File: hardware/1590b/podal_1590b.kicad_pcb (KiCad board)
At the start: 2 copper layers, 55 x 84 mm, 56 parts, among them J1 Guitar in, J2 fsw pin 1, J3 fsw pin 2, J4 fsw pin 4, J5 fsw pin 5, J6 fsw pin 6, J7 Left out, J8 Right out, J9 fsw pin 3, SW1 Switch 1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

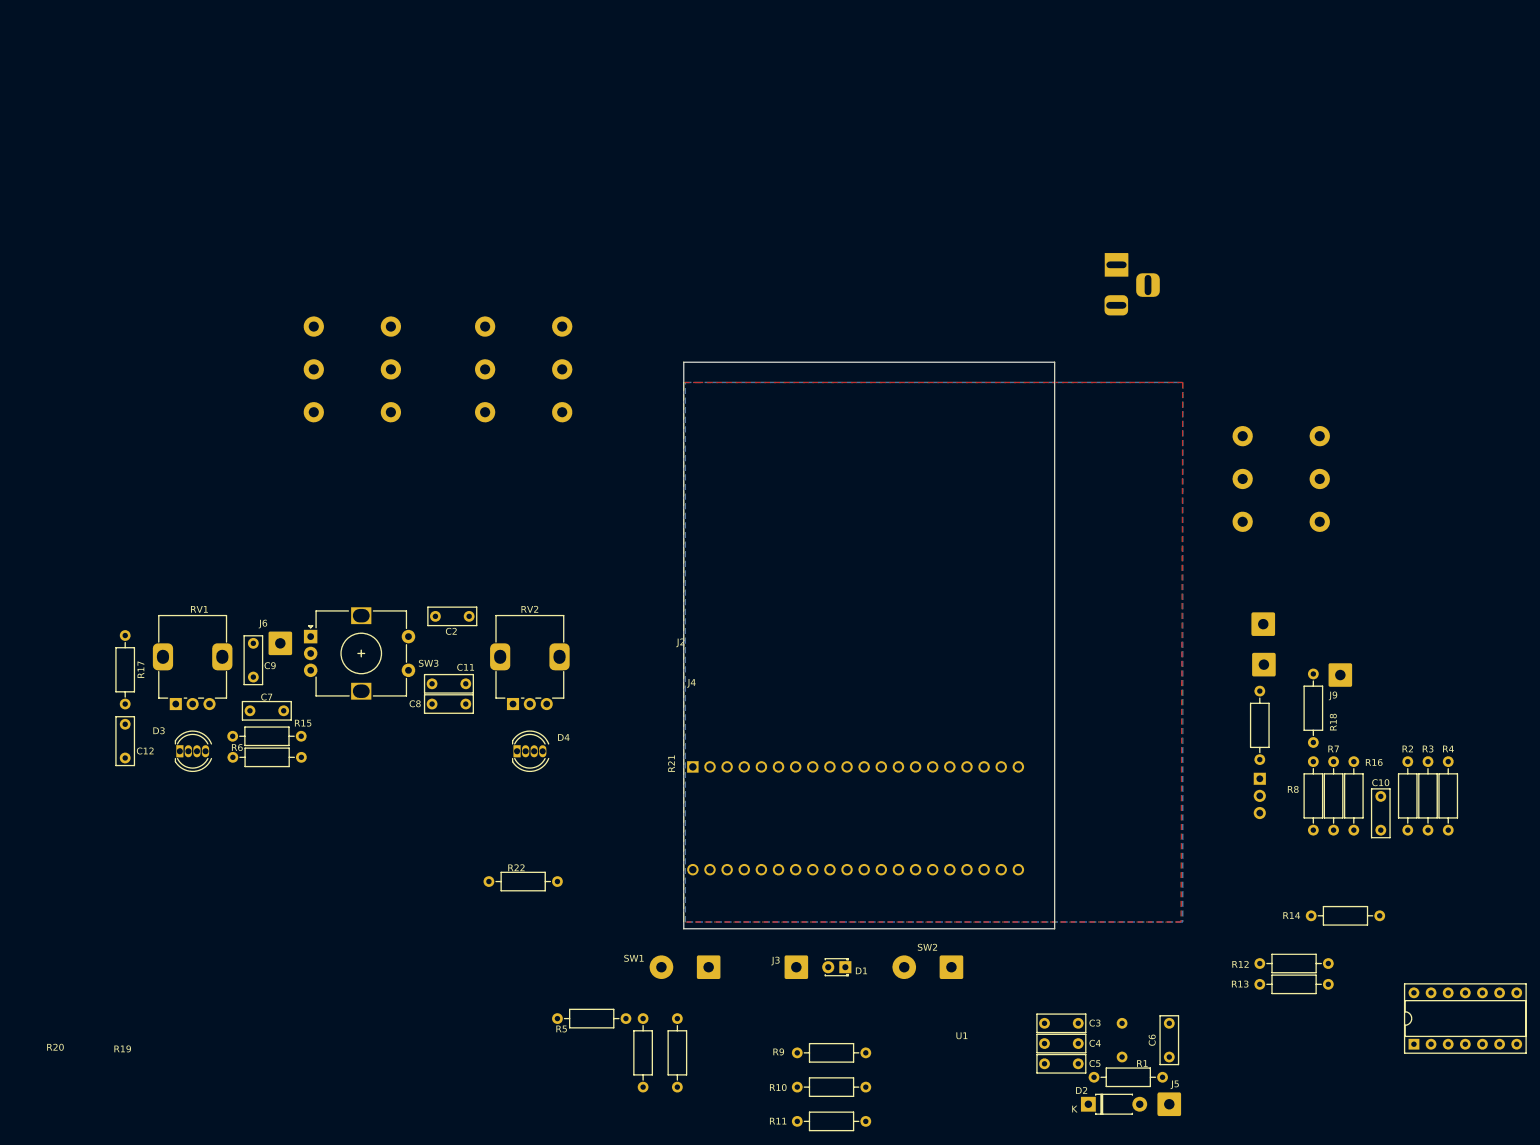
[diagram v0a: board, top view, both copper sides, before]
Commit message: Compressor working with sensible led output
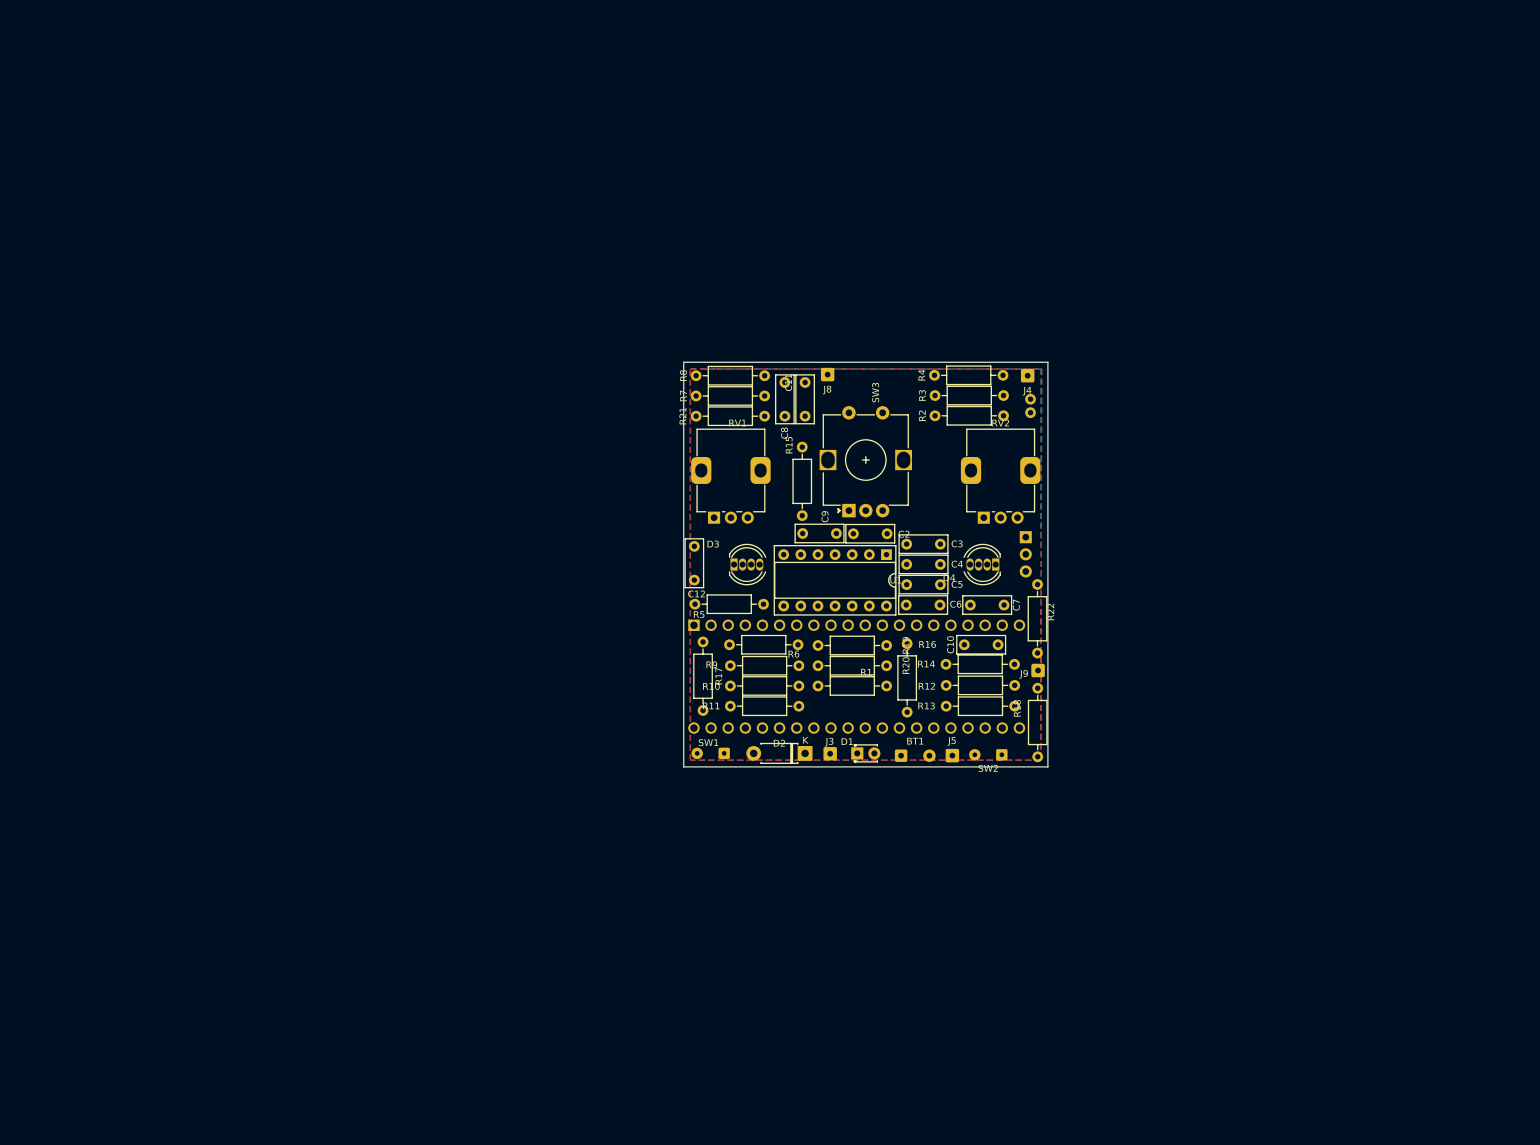
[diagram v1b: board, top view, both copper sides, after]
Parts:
- removed J1: Guitar in, Connector_Audio:Jack_6.35mm_Neutrik_NRJ6HM-1_Horizontal
- removed J2: fsw pin 1, Connector_Wire:SolderWire-0.75sqmm_1x01_D1.25mm_OD3.5mm
- removed J6: fsw pin 6, Connector_Wire:SolderWire-0.75sqmm_1x01_D1.25mm_OD3.5mm
- removed J7: Left out, Connector_Audio:Jack_6.35mm_Neutrik_NRJ6HM-1_Horizontal
- BT1: footprint Connector_BarrelJack:BarrelJack_Horizontal_centre_negative -> Connector_Wire:SolderWire-0.25sqmm_1x02_P4.2mm_D0.65mm_OD1.7mm; moved to F.Cu
- C1: footprint Capacitor_THT:C_Radial_D10.0mm_H16.0mm_P5.00mm -> Capacitor_THT:C_Radial_D5.0mm_H11.0mm_P2.00mm
- J3, J4, J5, J9: footprint Connector_Wire:SolderWire-0.75sqmm_1x01_D1.25mm_OD3.5mm -> Connector_Wire:SolderWire-0.25sqmm_1x01_D0.65mm_OD2mm
- J8: footprint Connector_Audio:Jack_6.35mm_Neutrik_NRJ6HM-1_Horizontal -> Connector_Wire:SolderWire-0.25sqmm_1x01_D0.65mm_OD2mm; moved to F.Cu
- SW1, SW2: footprint Connector_Wire:SolderWire-0.75sqmm_1x02_P7mm_D1.25mm_OD3.5mm -> Connector_Wire:SolderWire-0.15sqmm_1x02_P4mm_D0.5mm_OD1.5mm
- moved R7 109.0 mm to (101.8, 55.0), turned to 0 degrees
- moved C7 108.0 mm to (147.5, 86.0)
- moved U1 106.7 mm to (130.1, 78.5), turned to -90 degrees
- moved R8 105.6 mm to (112.0, 52.0), turned to 180 degrees
- moved R21 97.9 mm to (101.8, 58.0), turned to 0 degrees
- moved R4 95.3 mm to (137.2, 51.9), turned to 0 degrees
- moved C1 93.5 mm to (151.4, 55.5)
- moved R3 91.0 mm to (137.3, 54.9), turned to 0 degrees
- moved R15 90.6 mm to (117.6, 72.7), turned to 90 degrees
- moved C9 89.0 mm to (122.6, 75.4), turned to 180 degrees
- moved C12 88.4 mm to (101.6, 82.3)
- moved D3 86.7 mm to (107.5, 80.0)
- moved R2 85.8 mm to (147.4, 57.9), turned to 180 degrees
- moved R17 85.7 mm to (102.9, 91.5)
- moved RV1 84.5 mm to (104.5, 73.0)
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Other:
- board size 55 x 84 mm -> 54 x 60 mm
- board text added: "Podal v0.3 Denis Crowdy"
- board text removed: "Podal v0.2 Denis Crowdy"

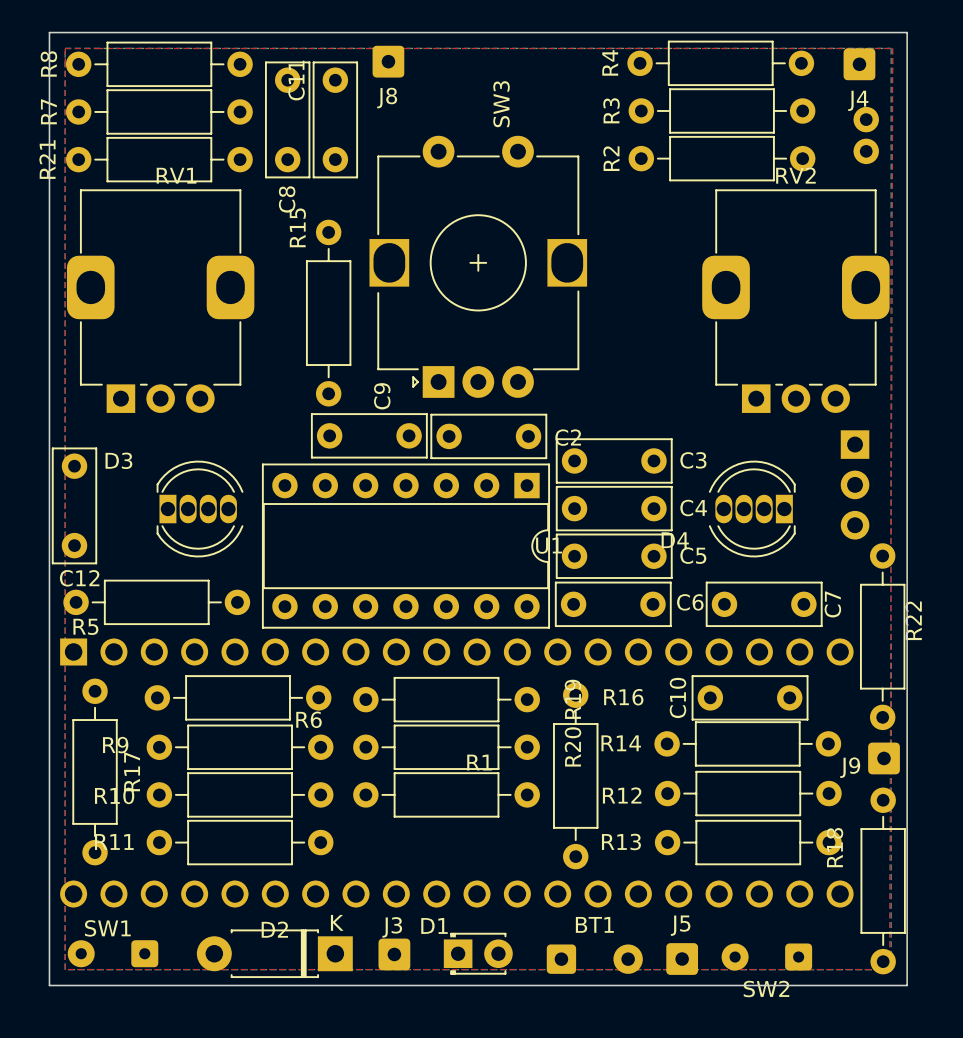
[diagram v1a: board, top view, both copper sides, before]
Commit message: Start work on connecting traces
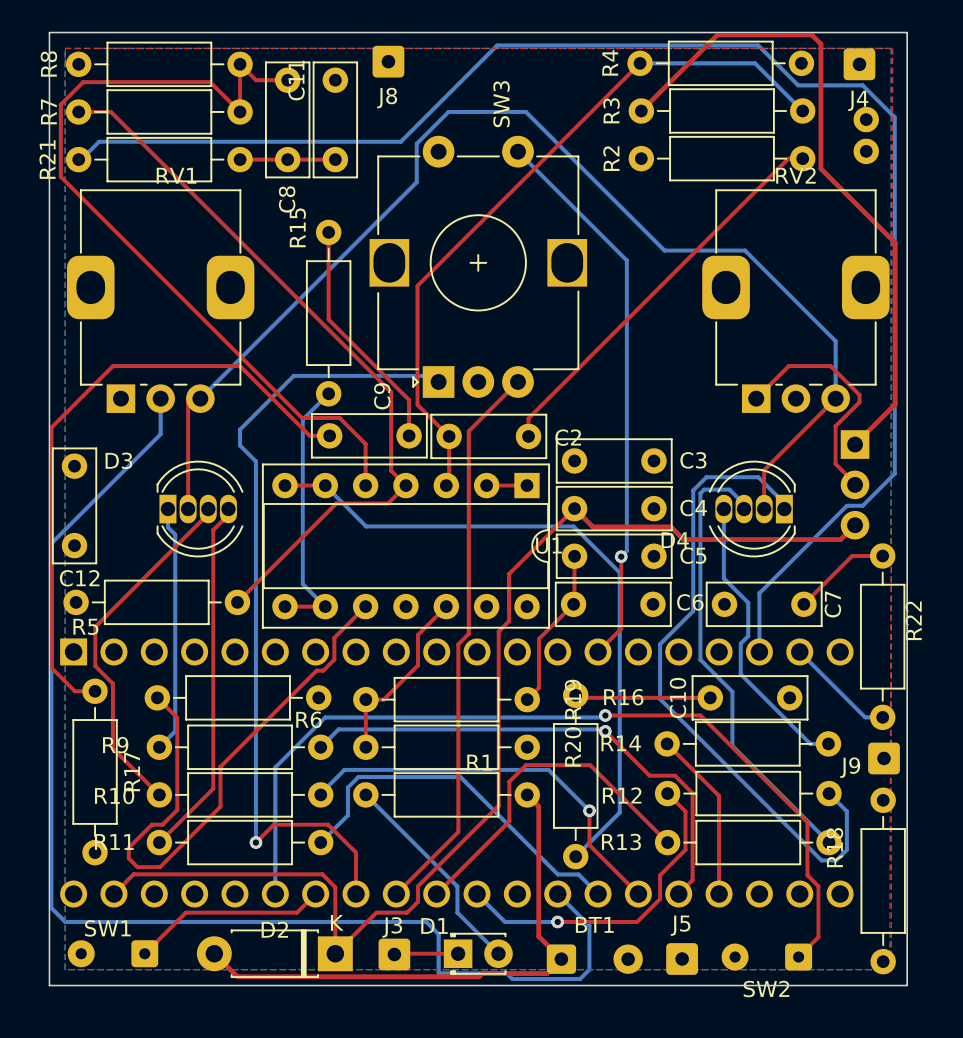
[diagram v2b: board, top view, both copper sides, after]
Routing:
- net +5V: track 0.00 -> 98.9 mm
- net /Left out: track 0.00 -> 94.0 mm
- net Net-(A1-ADC_6): track 0.00 -> 77.9 mm
- net /VCC: track 0.00 -> 75.4 mm
- net /3v3: track 0.00 -> 74.9 mm
- net Net-(A1-SAI2_SCK): track 0.00 -> 54.9 mm, vias 0 -> 1
- net Net-(U1B-+): track 0.00 -> 52.4 mm
- net Net-(A1-SAI2_SD_A): track 0.00 -> 51.5 mm, vias 0 -> 1
- net Net-(U1A-+): track 0.00 -> 44.8 mm
- net Net-(U1B--): track 0.00 -> 42.4 mm
- net Net-(D4-RK): track 0.00 -> 41.4 mm
- net Net-(C9-Pad2): track 0.00 -> 39.4 mm
- net Net-(U1C-+): track 0.00 -> 37.0 mm
- net Net-(A1-SAI2_SD_B): track 0.00 -> 35.4 mm
- net /ENC_CLICK: track 0.00 -> 35.1 mm, vias 0 -> 1
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
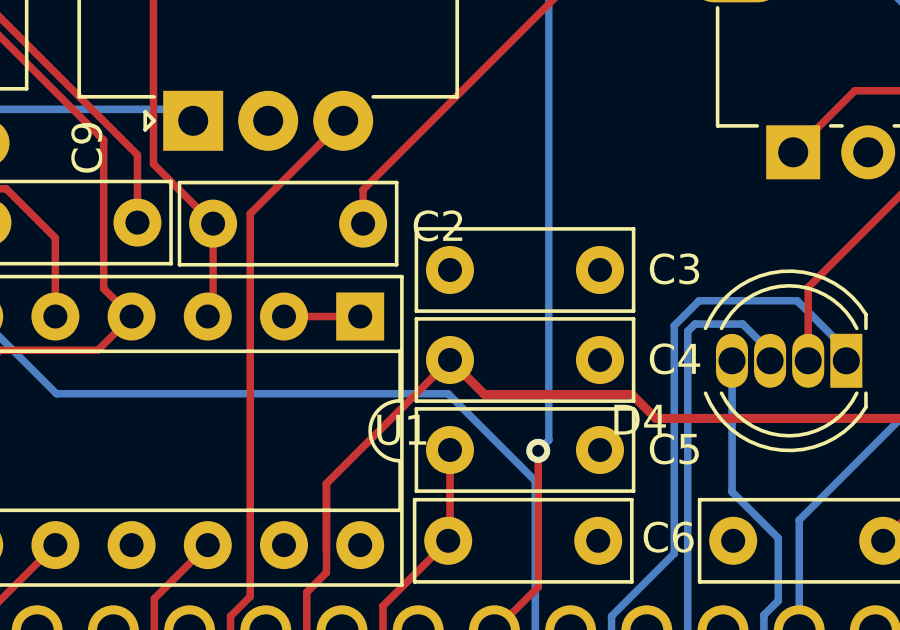
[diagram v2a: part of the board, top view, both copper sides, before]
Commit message: See if we can get some icad compatibility between mac and linux
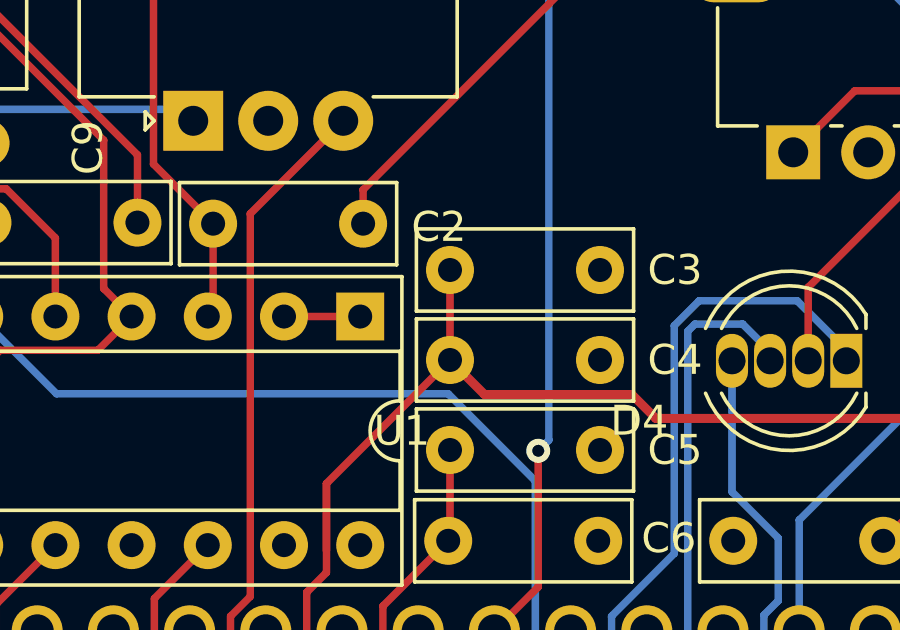
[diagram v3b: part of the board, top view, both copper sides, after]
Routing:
- net /VCC: track 75.4 -> 78.4 mm

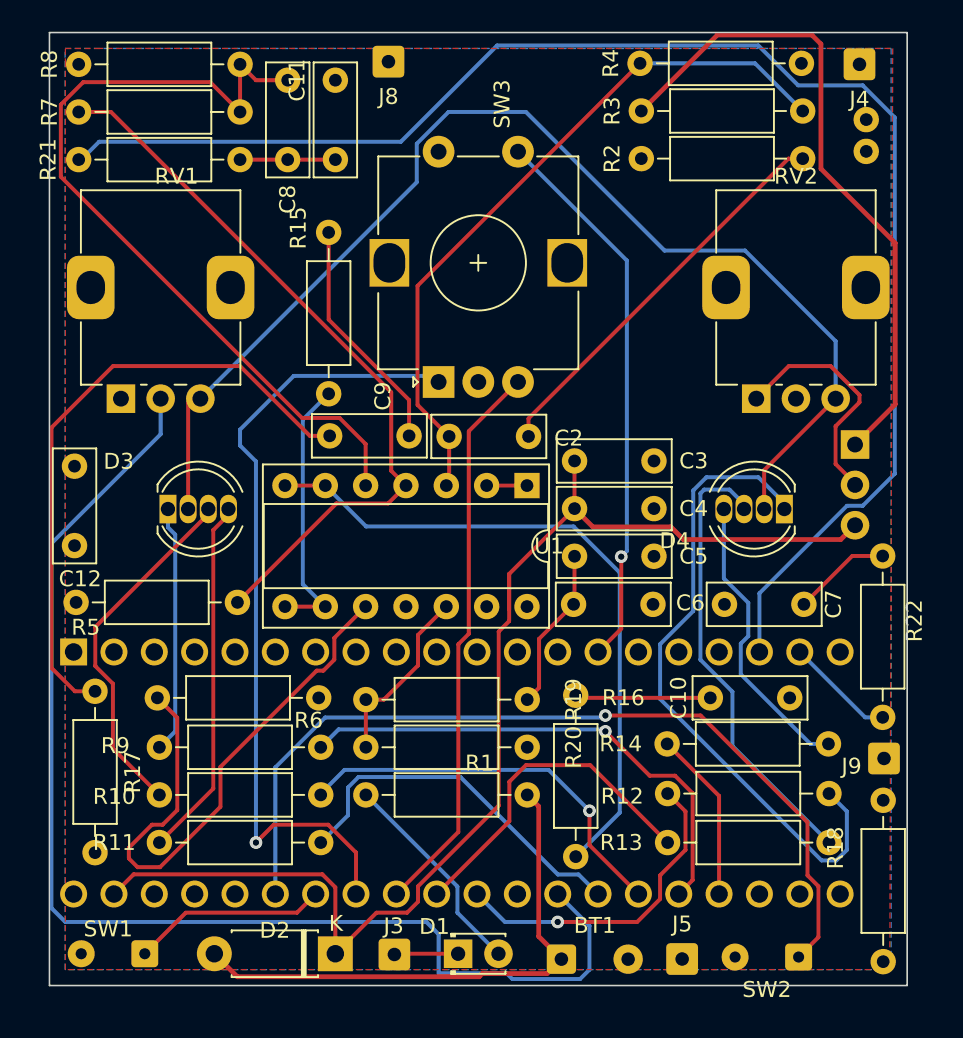
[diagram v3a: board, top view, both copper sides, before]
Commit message: Connect everything together
Board seems messy but good experiment with so many vias?
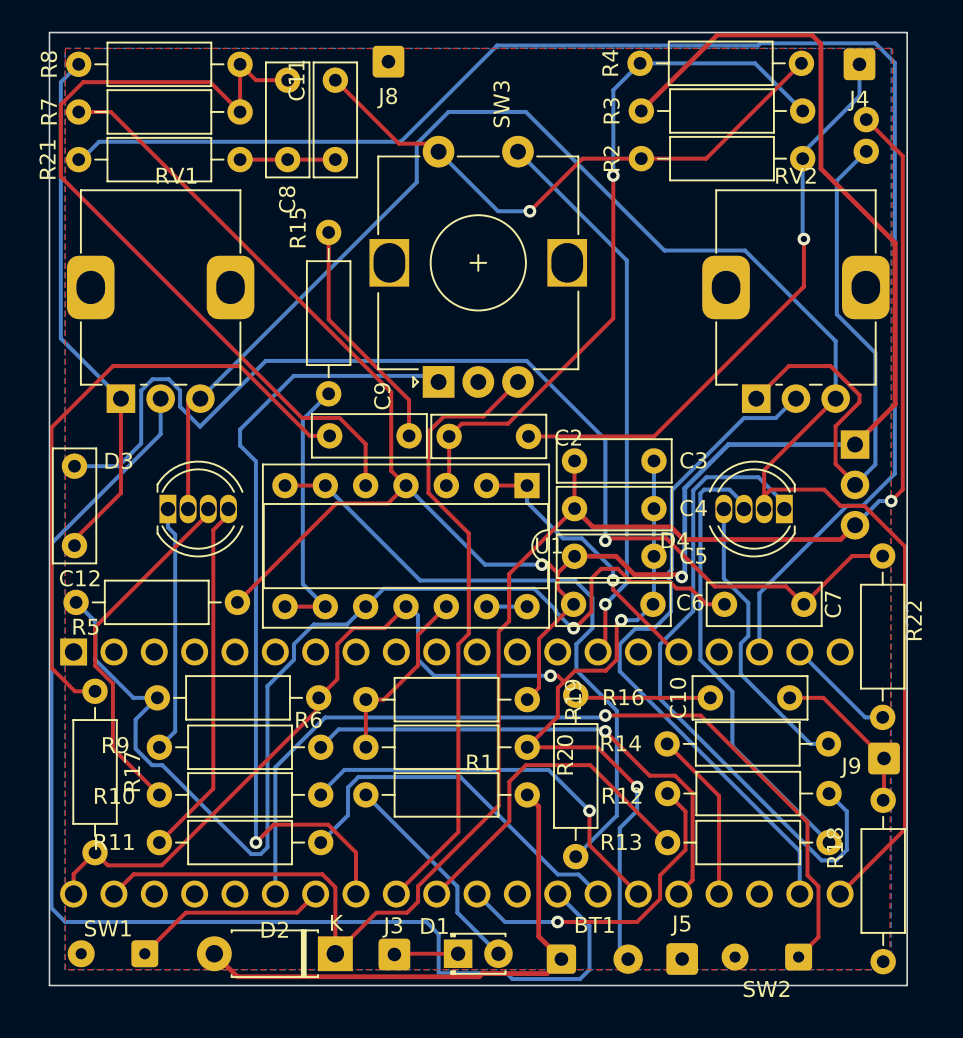
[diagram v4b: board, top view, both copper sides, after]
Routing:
- net GND: track 14.9 -> 196.5 mm, vias 0 -> 4
- net Net-(C12-Pad2): track 6.22 -> 70.1 mm, vias 0 -> 1
- net Net-(A1-ADC_0): track 0.00 -> 42.5 mm
- net +5V: track 98.9 -> 136.4 mm, vias 0 -> 2
- net /3v3: track 74.9 -> 109.8 mm
- net Net-(U1C-+): track 37.0 -> 71.4 mm, vias 0 -> 1
- net /VCC: track 78.4 -> 106.6 mm, vias 0 -> 1
- net /Left in: track 2.54 -> 17.8 mm, vias 0 -> 1
- net Net-(J4-Pin_1): track 25.2 -> 36.8 mm, vias 0 -> 1
- net Net-(J9-Pin_1): track 0.00 -> 10.5 mm
- net Net-(A1-SAI2_SD_B): track 35.4 -> 39.0 mm
- net Net-(U1D--): track 0.00 -> 2.54 mm
- net /Left out: track 94.0 -> 96.1 mm
- net Net-(U1B--): track 42.4 -> 41.1 mm
- net Net-(U1A-+): vias 0 -> 1
